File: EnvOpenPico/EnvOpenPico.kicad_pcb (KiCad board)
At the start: 2 copper layers, 21.1 x 51.3 mm, 35 parts, among them J2 SKRKAEE020, J3 2.54mm header 01x20, J4 2.54mm header 01x20, J5 Conn_01x03_Male, U1 TPS63002, U3 RP2040, X1 XO 32 12Mhz 3225 seiko

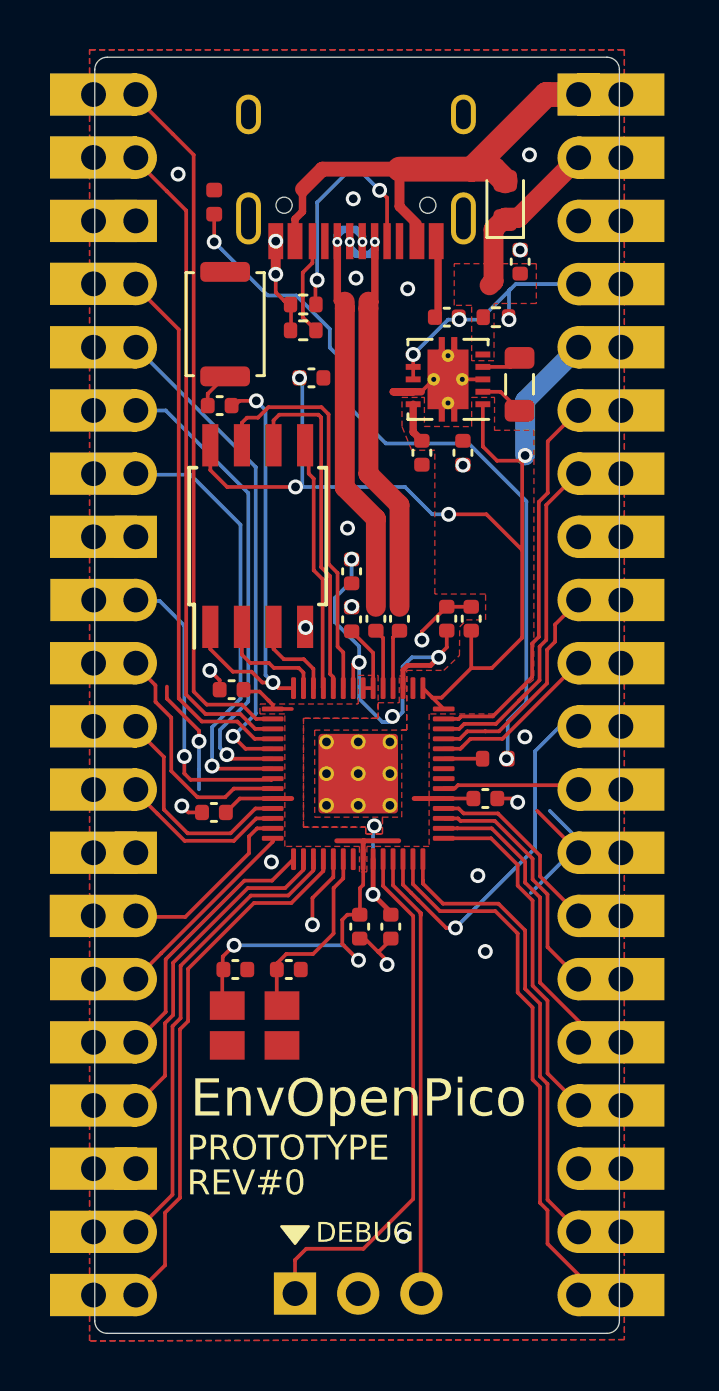
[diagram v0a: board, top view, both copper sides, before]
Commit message: small corrections and added a couple test points.
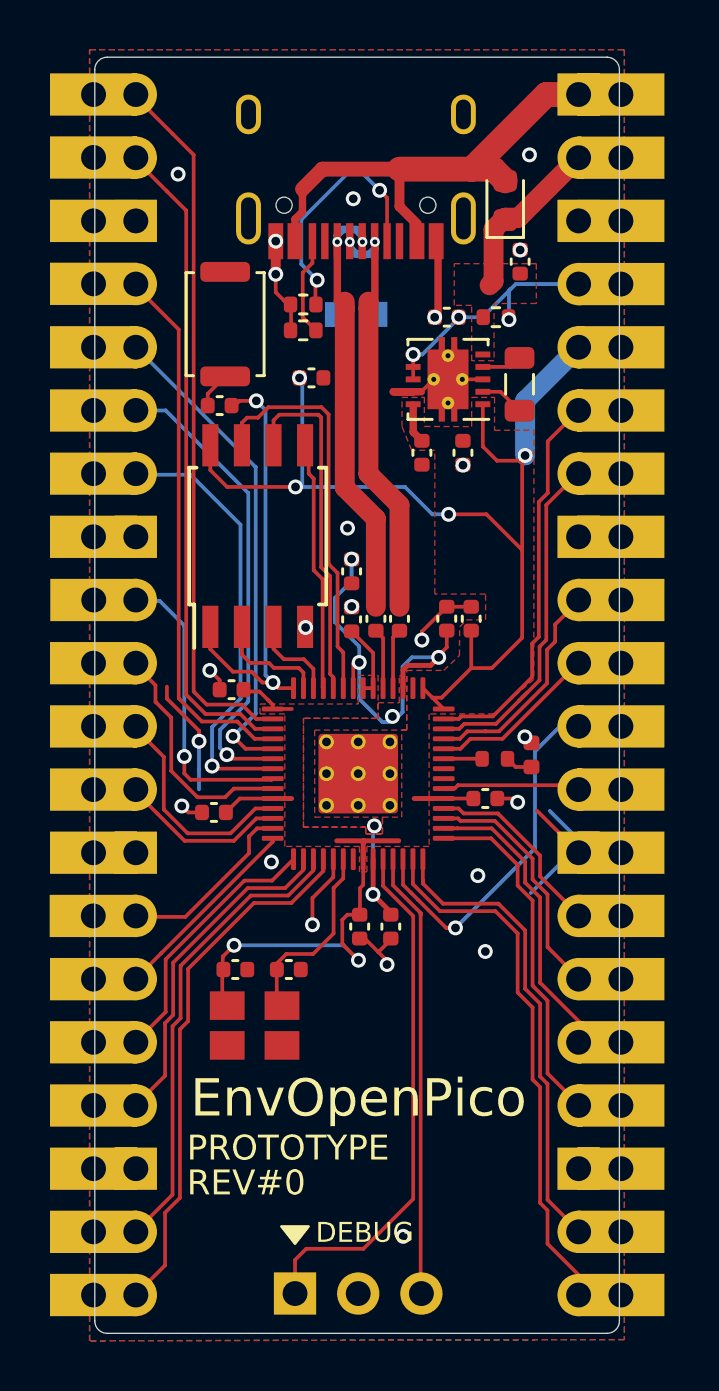
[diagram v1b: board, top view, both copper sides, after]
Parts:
- added TP1: TestPoint, TestPoint:TestPoint_Pad_1.0x1.0mm, B.Cu at (104.4, 67.6)
- added TP2: TestPoint, TestPoint:TestPoint_Pad_1.0x1.0mm, B.Cu at (102.9, 67.6)
- moved D3 25.6 mm to (110.7, 85.3)
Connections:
- R3 pad 1: /USB_D+ -> USB_D+
- R4 pad 1: /USB_D- -> USB_D+
- U3 pad 21: /XOUT -> (no net)
- U3 pad 35: /GPIO23 -> (no net)
- U3 pad 36: /GPIO24 -> (no net)
- X1 pad 1: Net-(X1-Pad1) -> (no net)
- e1 pad 3: Net-(e1-Pad3) -> (no net)
- e1 pad 5: /USB_D- -> USB_D+
- e1 pad 6: /USB_D+ -> USB_D+
- e1 pad 7: /USB_D- -> USB_D+
- e1 pad 8: /USB_D+ -> USB_D+
- e1 pad 9: Net-(e1-Pad9) -> (no net)
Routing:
- net USB_D+: track 0.00 -> 40.5 mm, vias 0 -> 4
- net Net-(D3-Pad2): track 30.0 -> 1.10 mm, vias 2 -> 0
- net /USB_D+: track 17.3 -> 0.00 mm, vias 2 -> 0
- net /USB_D-: track 17.3 -> 0.00 mm, vias 2 -> 0
- net GND: vias 24 -> 23

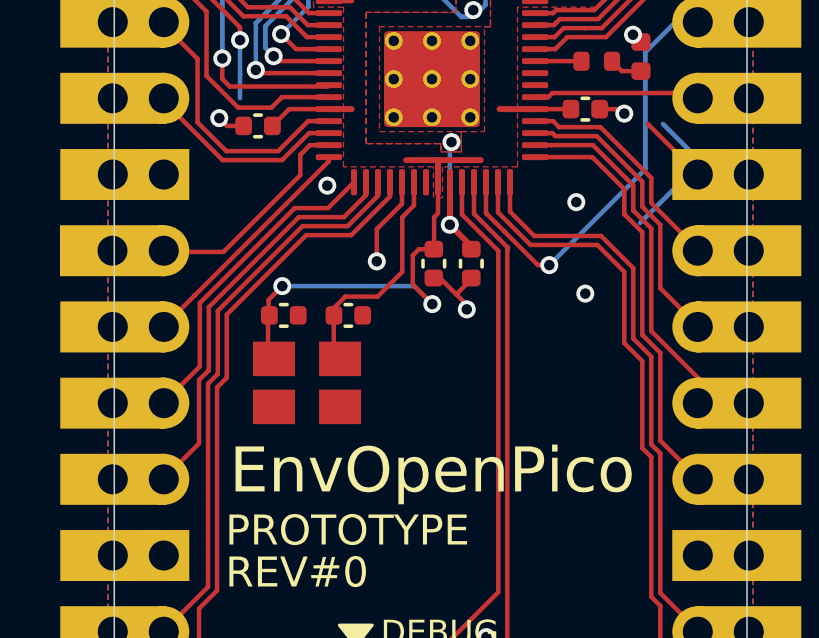
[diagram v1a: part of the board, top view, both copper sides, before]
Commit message: Rotated Oscillator by 180 degrees
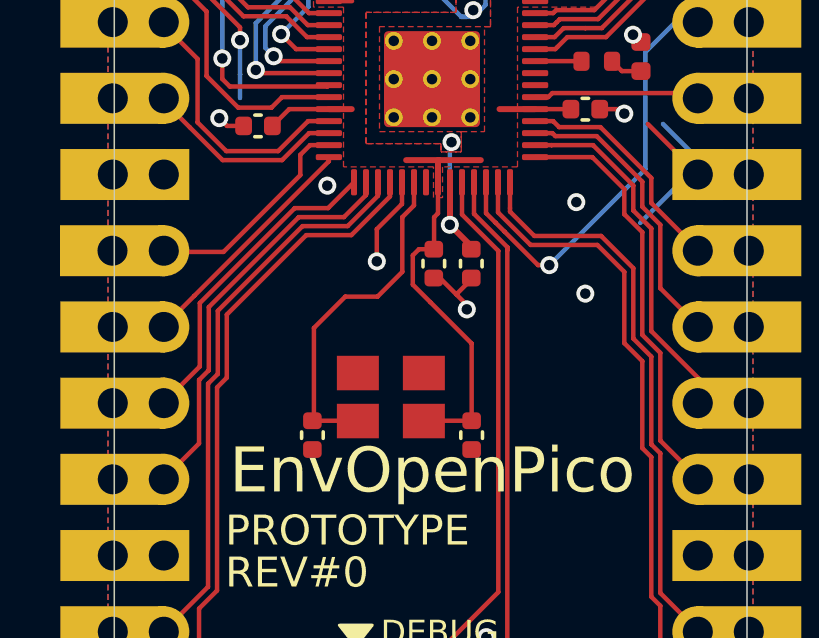
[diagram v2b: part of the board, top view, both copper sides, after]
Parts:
- moved C15 7.43 mm to (105.0, 97.9), turned to 270 degrees
- moved C2 4.17 mm to (99.7, 97.9), turned to 90 degrees
- moved X1 2.83 mm to (102.3, 96.6), turned to 180 degrees
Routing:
- net /XIN: track 7.62 -> 11.4 mm
- net +3V3: track 71.2 -> 69.2 mm, vias 6 -> 4

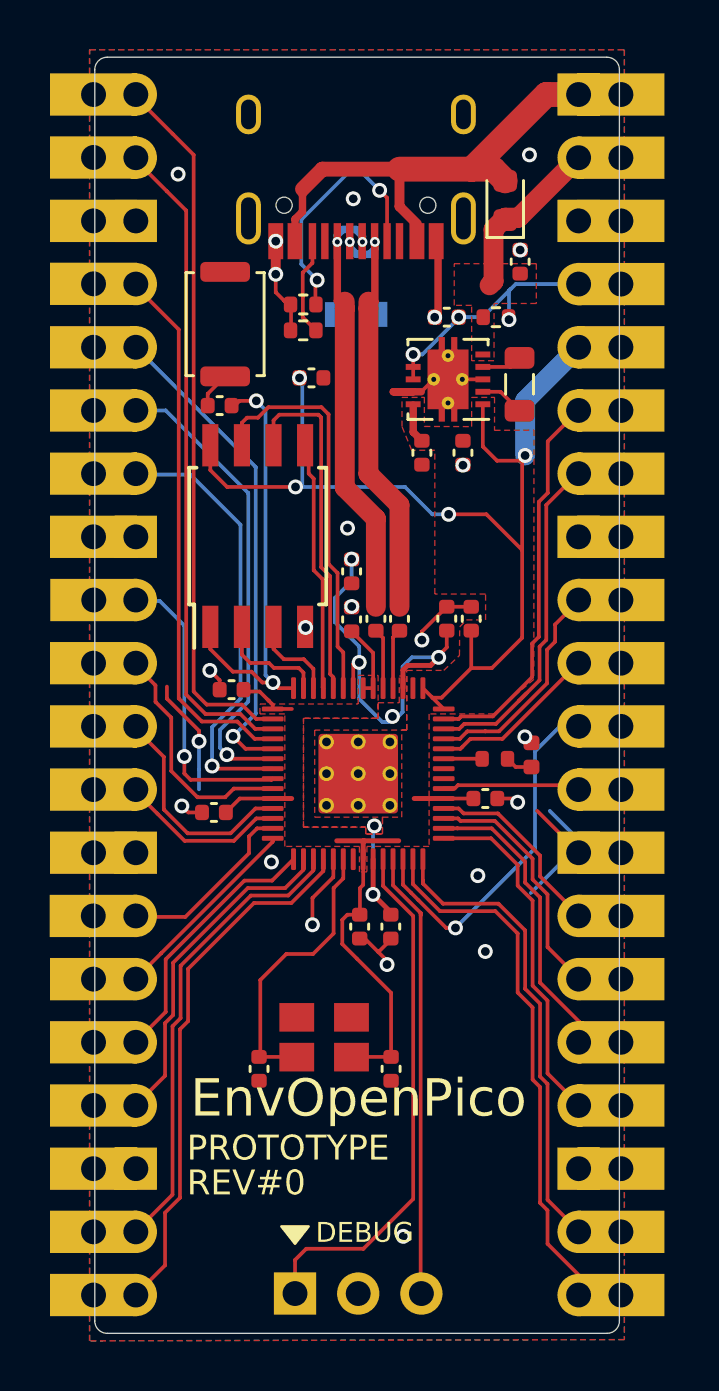
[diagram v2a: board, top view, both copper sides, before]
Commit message: corrected reveresed usb debug pads, added gnd debug pad and incremented revision number.
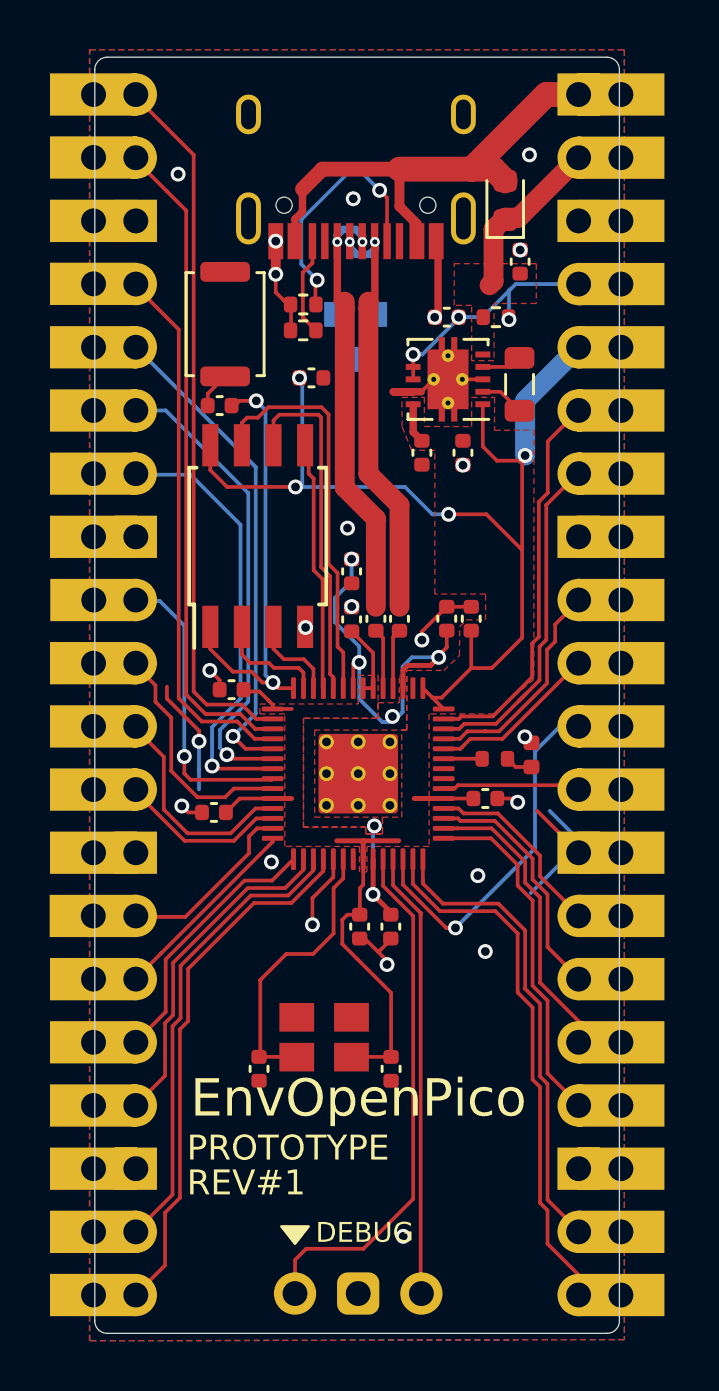
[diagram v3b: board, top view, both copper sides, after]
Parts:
- added TP3: TestPoint, TestPoint:TestPoint_Pad_1.0x1.0mm, B.Cu at (103.6, 69.4)
- moved TP1 1.53 mm to (102.8, 67.6)
- moved TP2 1.50 mm to (104.4, 67.6)
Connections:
- R4 pad 1: USB_D+ -> USB_D-
- TP2 pad 1: USB_D+ -> USB_D-
- e1 pad 5: USB_D+ -> USB_D-
- e1 pad 7: USB_D+ -> USB_D-
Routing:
- net USB_D-: track 0.00 -> 20.2 mm, vias 0 -> 2
- net USB_D+: track 40.5 -> 20.3 mm, vias 4 -> 2
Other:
- board text added: "REV#1"
- board text removed: "REV#0"

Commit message: Adjusted the placement of some components and added some filled zones.
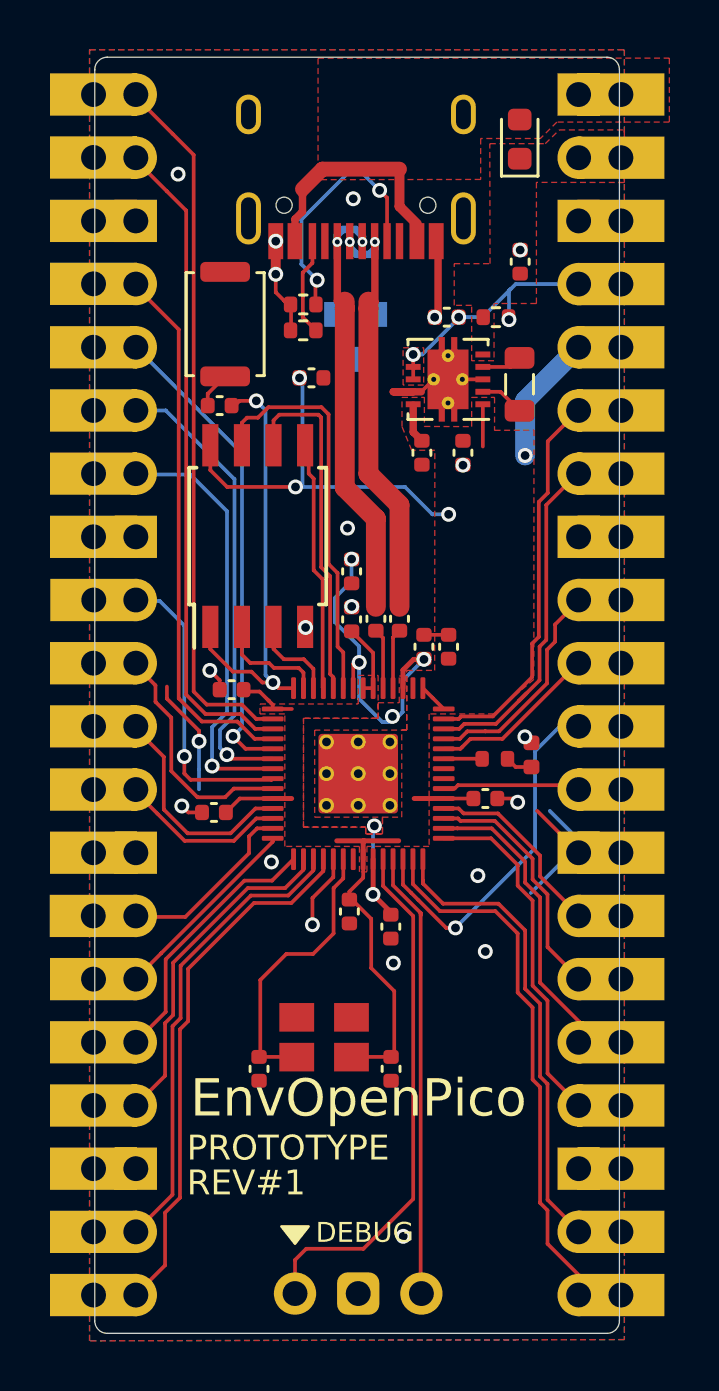
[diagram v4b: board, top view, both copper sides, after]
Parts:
- moved D1 2.53 mm to (110.2, 60.5)
- moved C7 1.46 mm to (106.3, 80.9)
- moved C10 1.45 mm to (107.3, 80.9)
- moved C14 0.74 mm to (103.3, 91.6)
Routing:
- net +3V3: track 69.2 -> 50.3 mm
- net VBUS: track 27.8 -> 10.7 mm
- net GND: track 34.6 -> 30.8 mm, vias 23 -> 21
- net +1V1: track 22.6 -> 19.9 mm
- added copper zone on F.Cu, net 3V3_EN

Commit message: moved some components to better locations and also created more filled areas
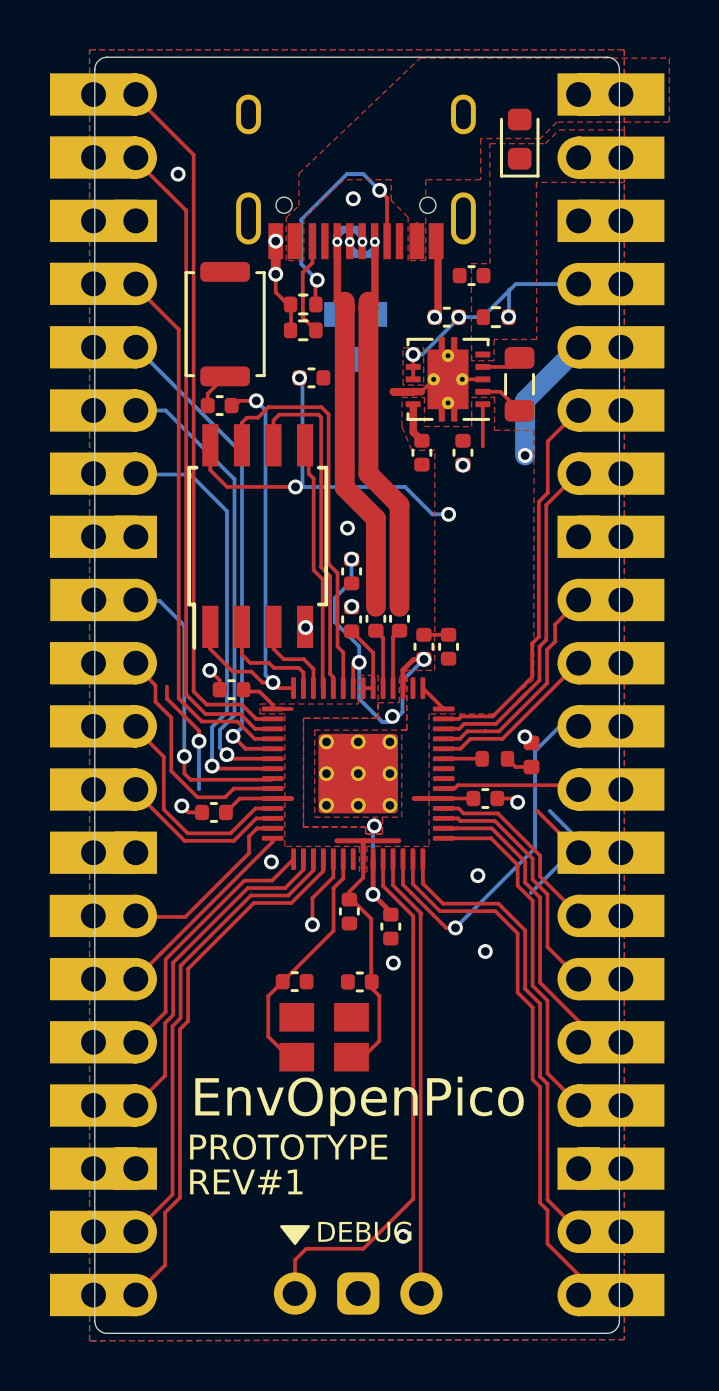
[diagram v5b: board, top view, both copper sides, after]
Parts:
- moved C2 3.79 mm to (101.1, 94.4), turned to 180 degrees
- moved C15 3.71 mm to (103.8, 94.4), turned to 180 degrees
- moved C1 2.03 mm to (108.2, 66.0), turned to 180 degrees
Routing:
- net VBUS: track 10.7 -> 1.72 mm
- net /XIN: track 11.4 -> 9.87 mm
- net +3V3: track 50.3 -> 49.1 mm
- net GND: vias 21 -> 20

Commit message: Hopefully implemented ADC_VREF Correctly on dip40 and pico verrsion
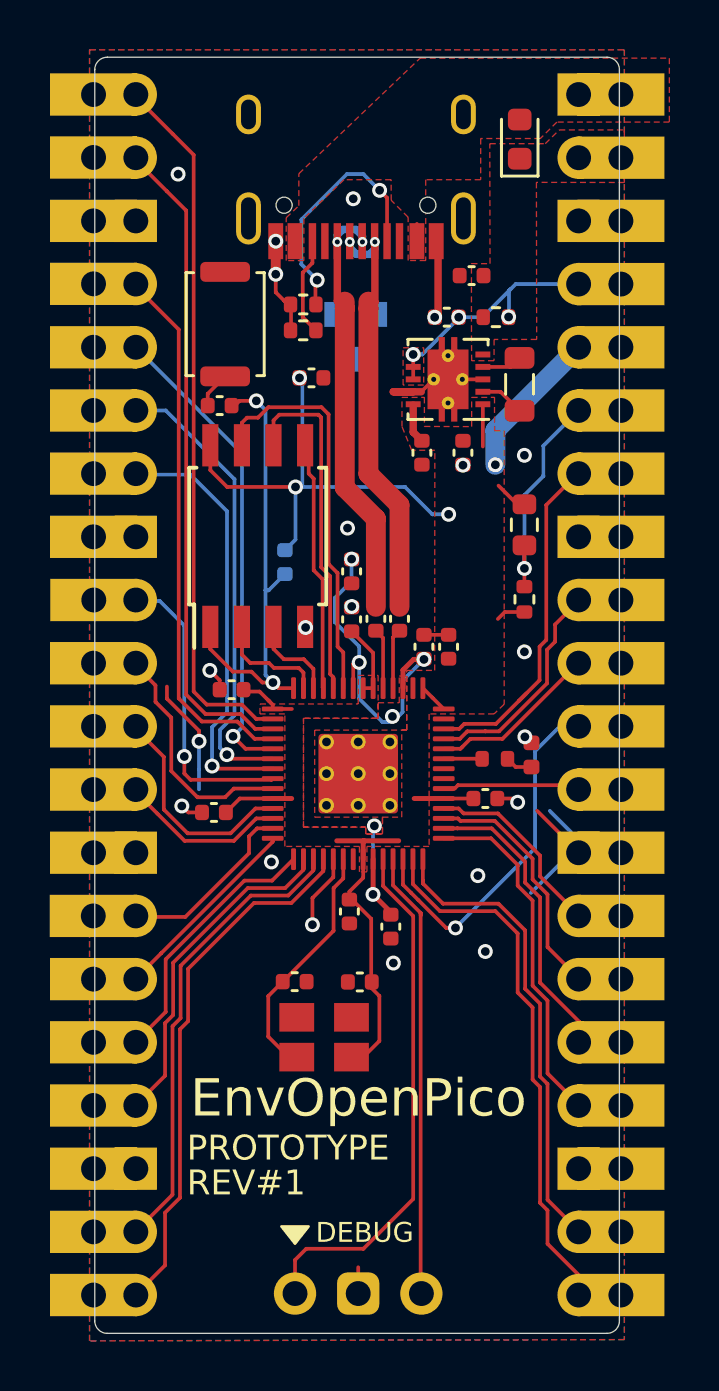
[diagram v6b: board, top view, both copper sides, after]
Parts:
- added R10: 1Ohm 0402, Resistor_SMD:R_0402_1005Metric, F.Cu at (110.4, 79.0)
- added R2: DNF, Capacitor_SMD:C_0402_1005Metric, B.Cu at (100.7, 77.5)
- added R9: 200ohm 0603, Resistor_SMD:R_0603_1608Metric, F.Cu at (110.4, 76.0)
- R1: value 1k Resistor -> 1k 0402 Resistor
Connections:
- J4 pad 6: /GPIO29_ADC3 -> /ADC_VREF
- U3 pad 41: /GPIO29_ADC3 -> (no net)
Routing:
- net /GPIO29_ADC3: track 16.5 -> 0.00 mm
- net /ADC_VREF: track 0.00 -> 9.66 mm, vias 0 -> 1
- net +3V3: track 49.1 -> 55.3 mm
- net GND: track 30.8 -> 31.8 mm, vias 20 -> 21
- net /QSPI_SS: track 17.6 -> 18.7 mm

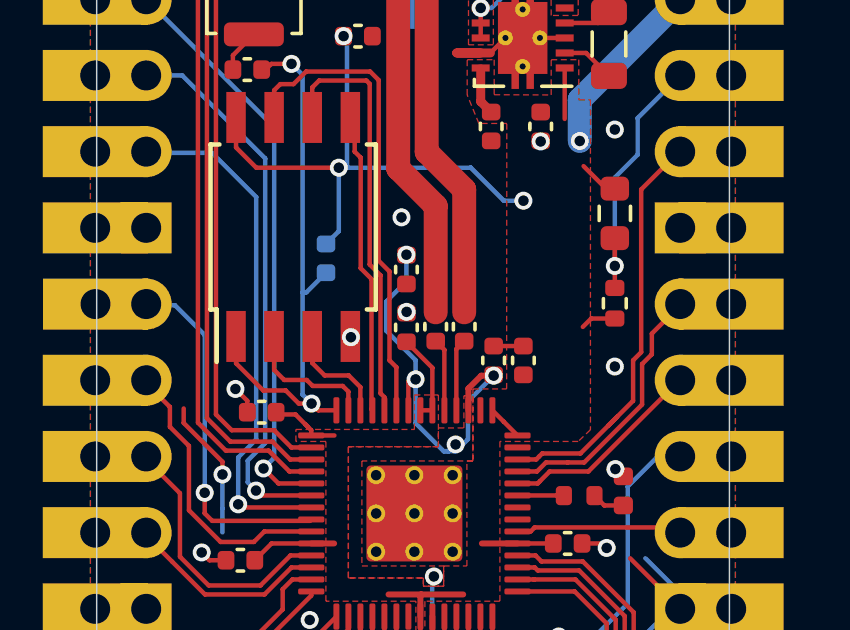
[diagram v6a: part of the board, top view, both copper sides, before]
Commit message: updated readme and corrected a capacitor placement.
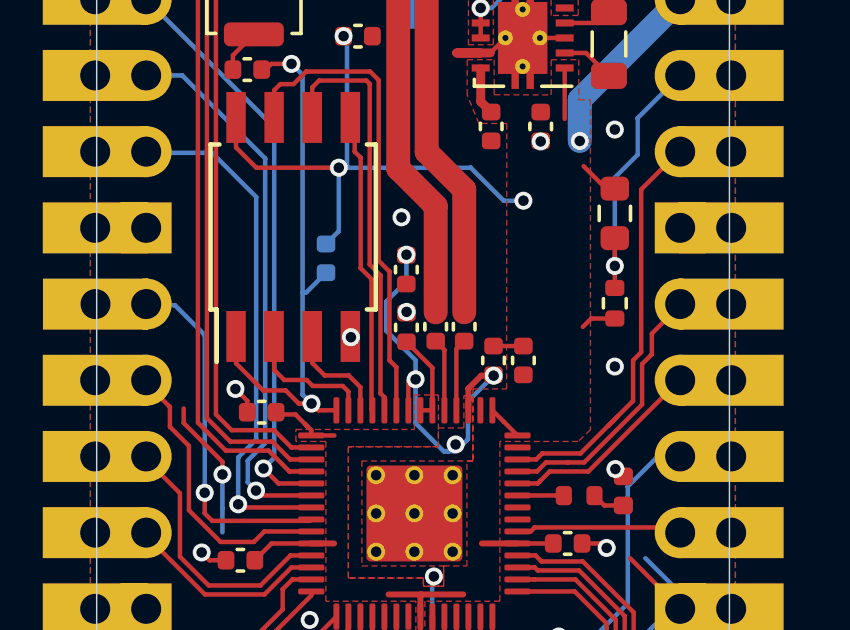
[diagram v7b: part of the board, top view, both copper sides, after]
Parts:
- moved C7 4.20 mm to (103.4, 77.9), turned to 270 degrees
- moved C3 4.20 mm to (106.3, 80.9), turned to 90 degrees
